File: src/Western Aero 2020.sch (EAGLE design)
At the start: 85 parts, among them U1 7806, U2 7805, U3 TEENSY_3.5_DIL+4, U5 SPARKFUN_MPU9250_IMU, U6 ADAFRUIT_MPL3115A2_BAROMETER, U7 ADAFRUIT_INA219_BATTERY_SENSOR, U8 ADAFRUIT_RFM95W_LORA_RADIO, U9 ADAFRUIT_MTK3339_GPS

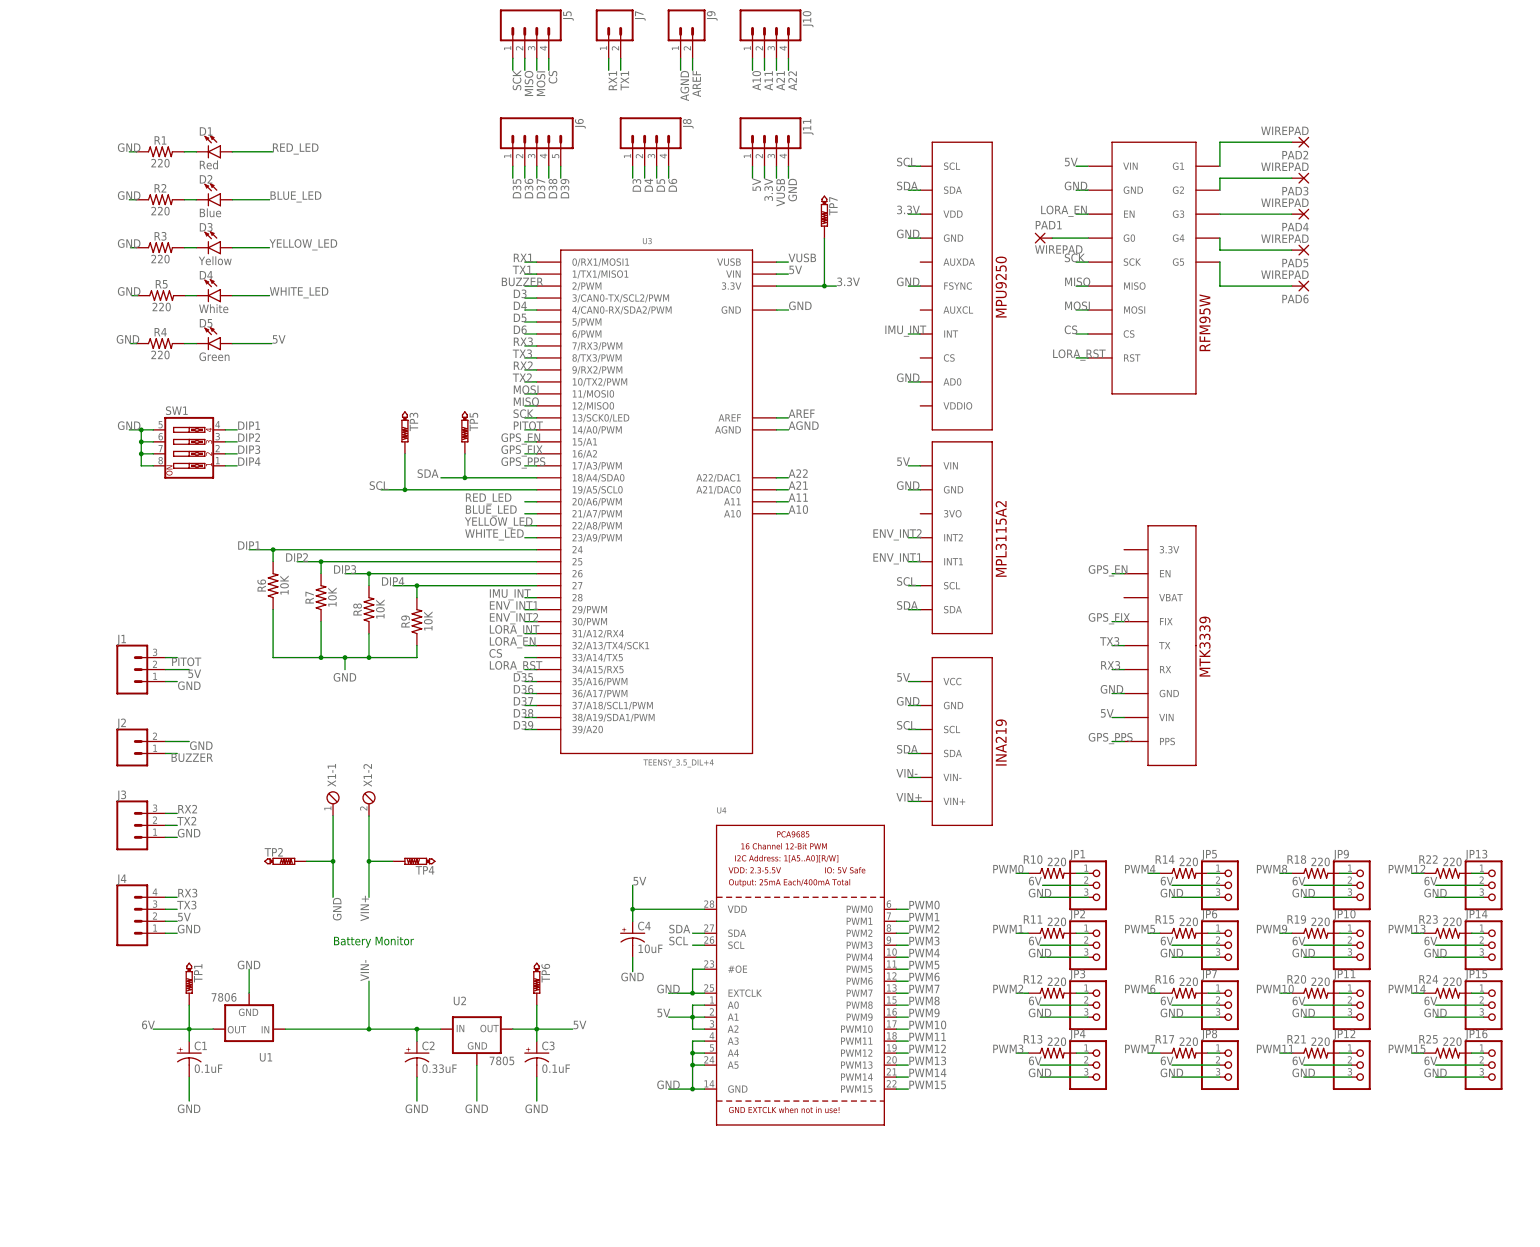
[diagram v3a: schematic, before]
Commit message: Add new voltage regulator
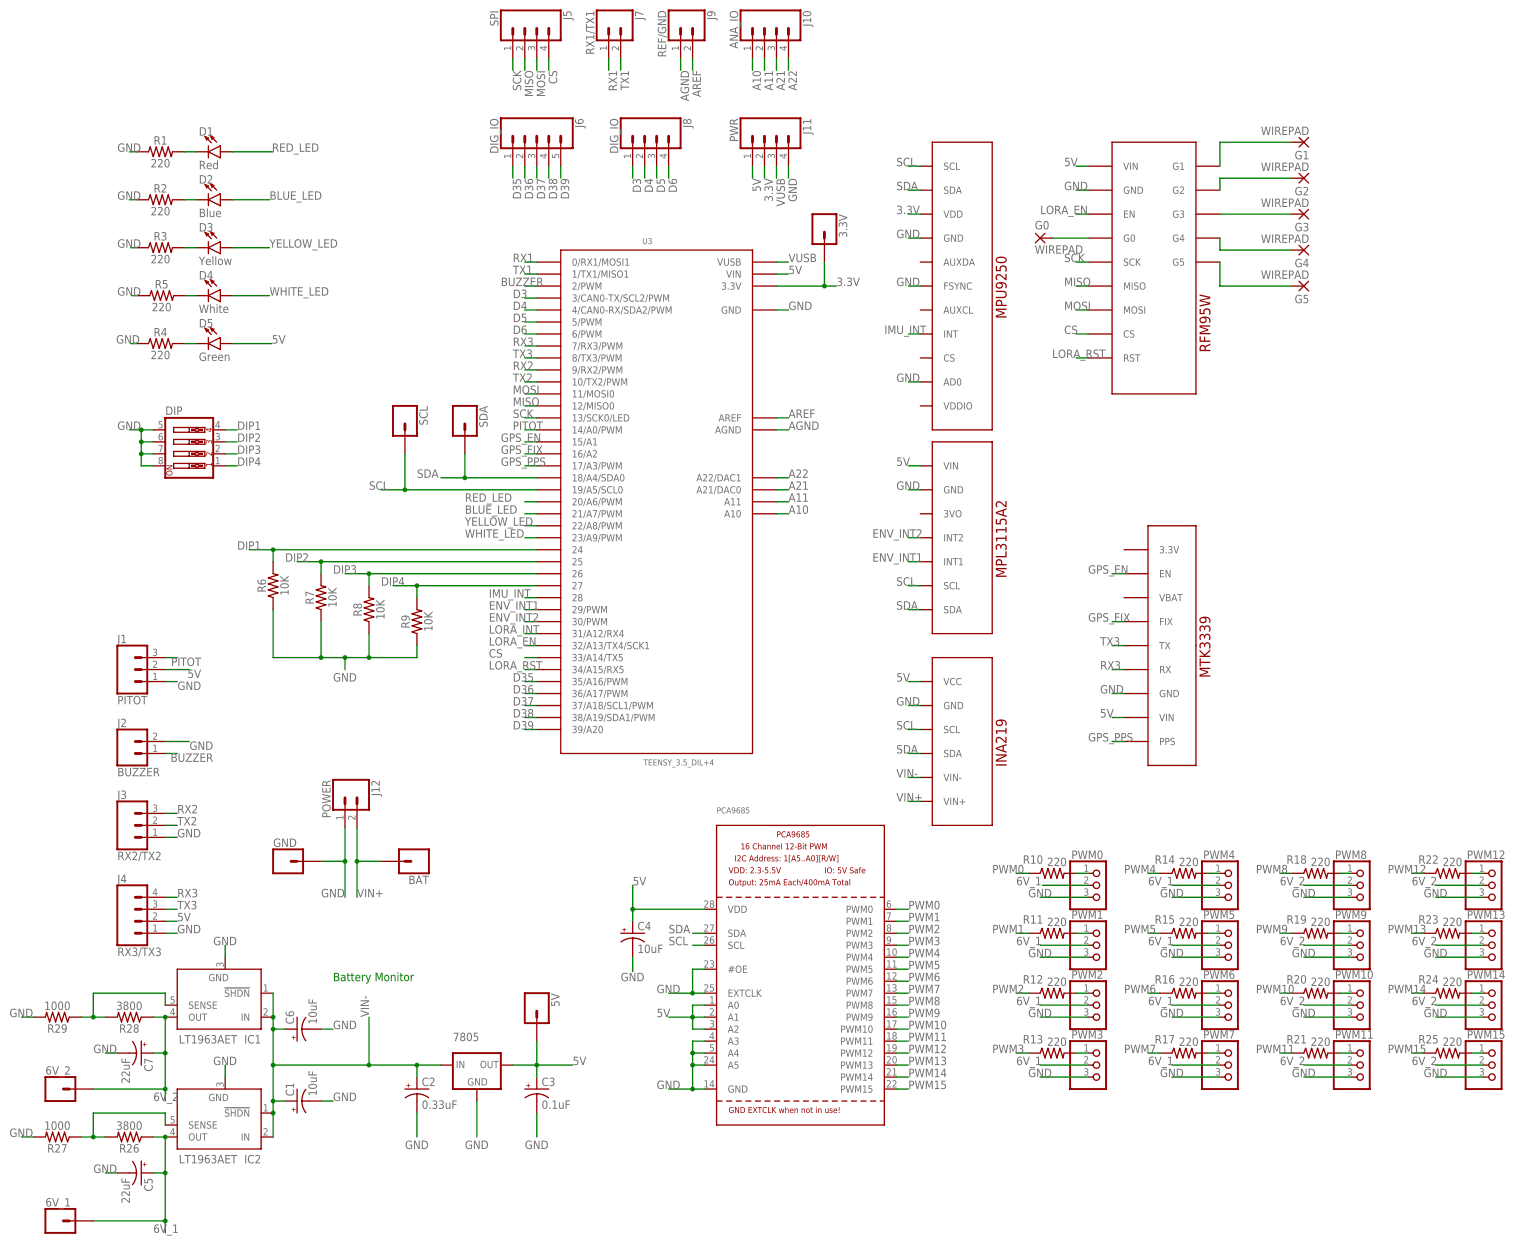
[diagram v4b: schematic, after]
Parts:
- removed TP1, TP2, TP3, TP4, TP5, TP6, TP7: PTR1PAD1-13, testpad:PTR1PAD1-13
- removed U1: 7806, SparkFun-IC-Power:V_REG_78XXSINK
- removed U2: 7805, SparkFun-IC-Power:V_REG_78XXSINK
- removed X1: (no value), con-phoenix-254:MPT2
- added 3.3V, 5V, 6V_1, 6V_2, BAT, GND, SCL, SDA: (no value), SparkFun-Connectors:CONN_01
- added 7805: 7805, SparkFun-IC-Power:V_REG_78XXSINK
- added C5, C7: 22uF, SparkFun-Capacitors:10UF-POLAR-RADIAL-2.5MM-25V-20%
- added C6: 10uF, SparkFun-Capacitors:10UF-POLAR-RADIAL-2.5MM-25V-20%
- added IC1, IC2: LT1963AET, linear-technology:LT1963AET
- added J12: POWER, SparkFun-Connectors:CONN_02
- added R26, R28: 3800, SparkFun-Resistors:330OHM-HORIZ-1/10W-5%
- added R27, R29: 1000, SparkFun-Resistors:330OHM-HORIZ-1/10W-5%
- C1: value 0.1uF -> 10uF
- J1: value (none) -> PITOT
- J10: value (none) -> ANA_IO
- J11: value (none) -> PWR
- J2: value (none) -> BUZZER
- J3: value (none) -> RX2/TX2
- J4: value (none) -> RX3/TX3
- J5: value (none) -> SPI
- J6, J8: value (none) -> DIG_IO
- J7: value (none) -> RX1/TX1
- J9: value (none) -> REF/GND
- JP1: value (none) -> PWM0
- JP10: value (none) -> PWM9
- JP11: value (none) -> PWM10
- JP12: value (none) -> PWM11
- JP13: value (none) -> PWM12
- JP14: value (none) -> PWM13
- JP15: value (none) -> PWM14
- JP16: value (none) -> PWM15
- JP2: value (none) -> PWM1
- JP3: value (none) -> PWM2
- JP4: value (none) -> PWM3
- JP5: value (none) -> PWM4
- JP6: value (none) -> PWM5
- JP7: value (none) -> PWM6
- JP8: value (none) -> PWM7
- JP9: value (none) -> PWM8
- renumbered PAD1 to G0, PAD2 to G1, PAD3 to G2, PAD4 to G3, PAD5 to G4, PAD6 to G5, SW1 to DIP, U4 to PCA9685
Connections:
- removed net 6V: C1.+, JP1.2, JP10.2, JP11.2, JP12.2, JP13.2, JP14.2, JP15.2, JP16.2, JP2.2, JP3.2, JP4.2, JP5.2, JP6.2, JP7.2, JP8.2, JP9.2, TP1.TP, U1.OUT
- new net 6V_1: 6V_1.1, C5.+, IC2.OUT, JP1.2, JP2.2, JP3.2, JP4.2, JP5.2, JP6.2, JP7.2, JP8.2, R26.1
- new net 6V_2: 6V_2.1, C7.+, IC1.OUT, JP10.2, JP11.2, JP12.2, JP13.2, JP14.2, JP15.2, JP16.2, JP9.2, R28.1
- new net N$28: IC1.SENSE, R28.2, R29.1
- new net N$29: IC2.SENSE, R26.2, R27.1
- net 3.3V: now also 3.3V.1; no longer TP7.TP
- net 5V: now also 5V.1, 7805.OUT; no longer TP6.TP, U2.OUT
- net GND: now also 7805.GND, C5.-, C6.-, C7.-, GND.1, IC1.GND, IC2.GND, J12.1, R27.2, R29.2; no longer TP2.TP, U1.GND, U2.GND, X1-1.1
- net SCL: now also SCL.1; no longer TP3.TP
- net SDA: now also SDA.1; no longer TP5.TP
- net VIN+: now also BAT.1, J12.2; no longer TP4.TP, X1-2.1
- net VIN-: now also 7805.IN, C1.+, C6.+, IC1.!SHDN, IC1.IN, IC2.!SHDN, IC2.IN; no longer U1.IN, U2.IN
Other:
- moved on the sheet: C1, C2, C3

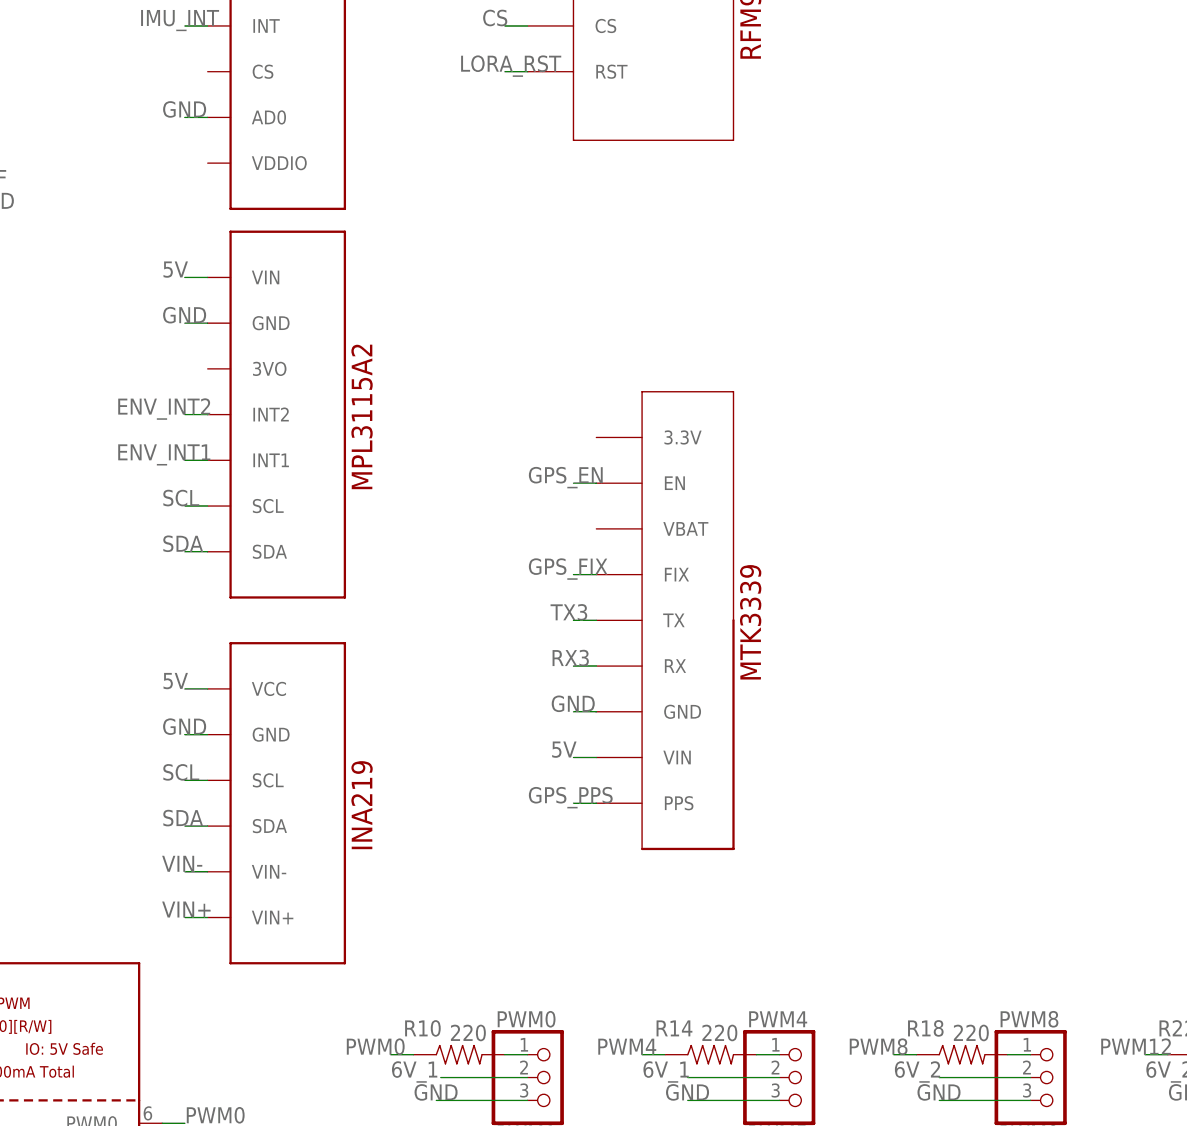
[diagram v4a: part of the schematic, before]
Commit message: Changed test point parts. Updated parts list. Adjusted board layout.
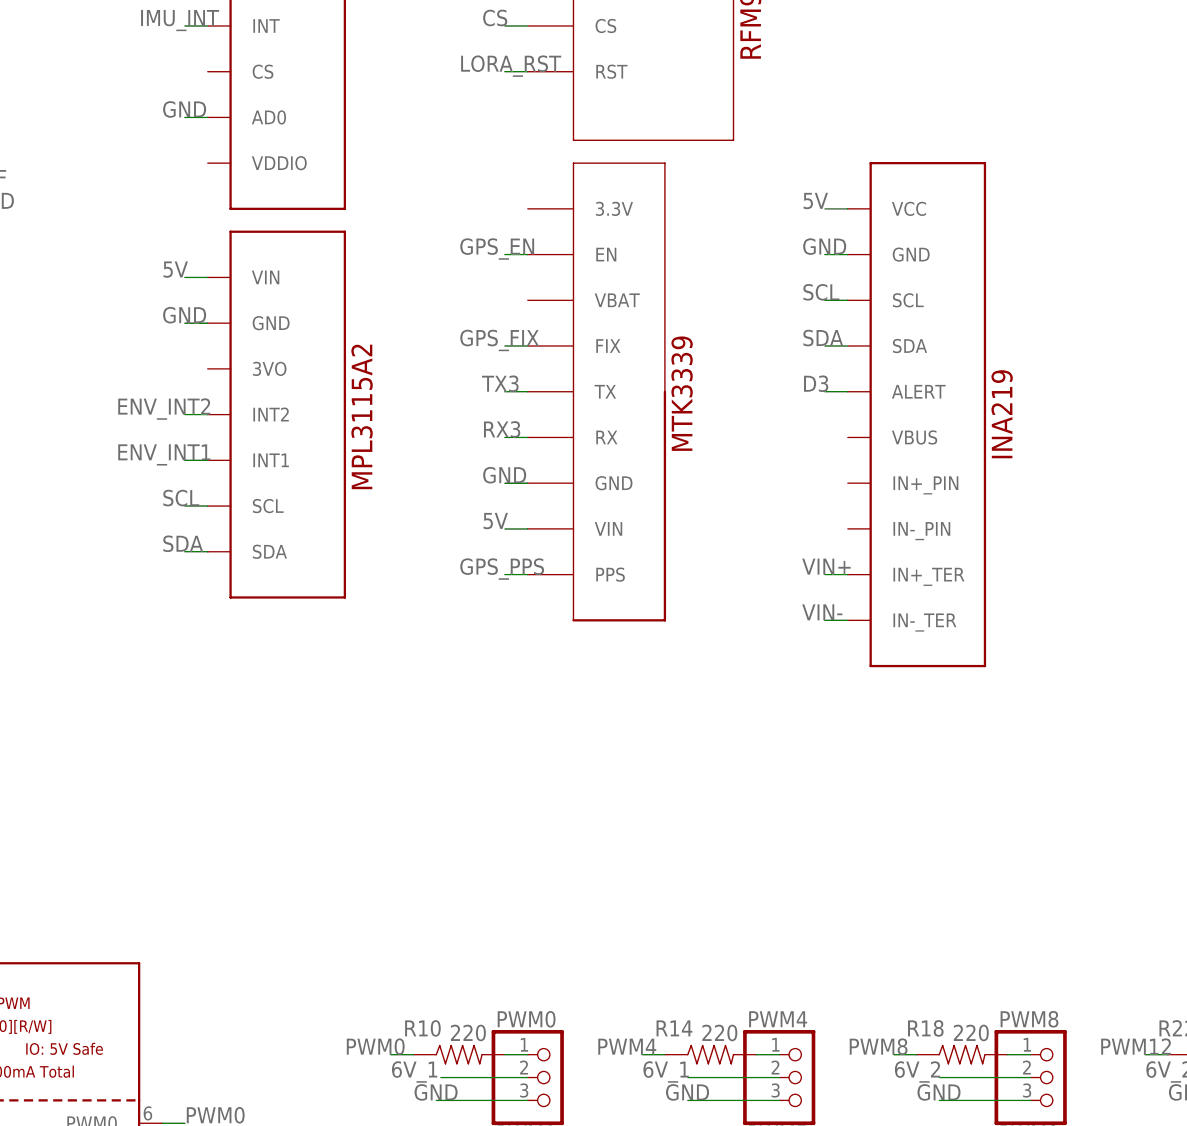
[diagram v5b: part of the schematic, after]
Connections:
- net D3: now also U7.ALERT
- net VIN+: now also U7.IN+_TER; no longer U7.VIN+
- net VIN-: now also U7.IN-_TER; no longer U7.VIN-
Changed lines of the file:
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@@
 <instance part="U8" gate="G$1" x="121.92" y="195.58" smashed="yes" rot="R270"/>
 <instance part="U6" gate="G$1" x="83.82" y="132.08" smashed="yes" rot="R270"/>
-<instance part="U7" gate="G$1" x="83.82" y="86.36" smashed="yes" rot="R270"/>
+<instance part="U7" gate="G$1" x="154.94" y="139.7" smashed="yes" rot="R270"/>
 <instance part="J2" gate="G$1" x="-86.36" y="66.04" smashed="yes">
 <attribute name="VALUE" x="-88.9" y="61.214" size="1.778" layer="96" font="vector"/>
@@
 <attribute name="NAME" x="-88.9" y="38.608" size="1.778" layer="95" font="vector"/>
 </instance>
-<instance part="U9" gate="G$1" x="137.16" y="114.3" smashed="yes" rot="R270"/>
+<instance part="U9" gate="G$1" x="129.54" y="139.7" smashed="yes" rot="R270"/>
 <instance part="J7" gate="G$1" x="15.24" y="220.98" smashed="yes" rot="R270">
 <attribute name="VALUE" x="10.414" y="223.52" size="1.778" layer="96" font="vector" rot="R270"/>
@@
 <nets>
 <net name="VIN+" class="0">
-<segment>
-<pinref part="U7" gate="G$1" pin="VIN+"/>
-<wire x1="81.28" y1="55.88" x2="78.74" y2="55.88" width="0.1524" layer="91"/>
-<label x="76.2" y="55.88" size="1.778" layer="95"/>
-</segment>
 <segment>
 <label x="-38.1" y="35.56" size="1.778" layer="95"/>
@@
 <junction x="-38.1" y="43.18"/>
 </segment>
+<segment>
+<pinref part="U7" gate="G$1" pin="IN+_TER"/>
+<wire x1="152.4" y1="93.98" x2="149.86" y2="93.98" width="0.1524" layer="91"/>
+<label x="147.32" y="93.98" size="1.778" layer="95"/>
+</segment>
 </net>
 <net name="3.3V" class="0">
@@
 <segment>
 <pinref part="U7" gate="G$1" pin="GND"/>
-<wire x1="81.28" y1="76.2" x2="78.74" y2="76.2" width="0.1524" layer="91"/>
-<label x="76.2" y="76.2" size="1.778" layer="95"/>
+<wire x1="152.4" y1="129.54" x2="149.86" y2="129.54" width="0.1524" layer="91"/>
+<label x="147.32" y="129.54" size="1.778" layer="95"/>
 </segment>
 <segment>
@@
 <segment>
 <pinref part="U9" gate="G$1" pin="GND"/>
-<wire x1="124.46" y1="78.74" x2="121.92" y2="78.74" width="0.1524" layer="91"/>
-<label x="119.38" y="78.74" size="1.778" layer="95"/>
+<wire x1="116.84" y1="104.14" x2="114.3" y2="104.14" width="0.1524" layer="91"/>
+<label x="111.76" y="104.14" size="1.778" layer="95"/>
 </segment>
 <segment>
@@
 <segment>
 <pinref part="U7" gate="G$1" pin="SDA"/>
-<wire x1="81.28" y1="66.04" x2="78.74" y2="66.04" width="0.1524" layer="91"/>
-<label x="76.2" y="66.04" size="1.778" layer="95"/>
+<wire x1="152.4" y1="119.38" x2="149.86" y2="119.38" width="0.1524" layer="91"/>
+<label x="147.32" y="119.38" size="1.778" layer="95"/>
 </segment>
 <segment>
@@
 <segment>
 <pinref part="U7" gate="G$1" pin="SCL"/>
-<wire x1="81.28" y1="71.12" x2="78.74" y2="71.12" width="0.1524" layer="91"/>
-<label x="76.2" y="71.12" size="1.778" layer="95"/>
+<wire x1="152.4" y1="124.46" x2="149.86" y2="124.46" width="0.1524" layer="91"/>
+<label x="147.32" y="124.46" size="1.778" layer="95"/>
 </segment>
 <segment>
@@
 <segment>
 <pinref part="U7" gate="G$1" pin="VCC"/>
-<wire x1="81.28" y1="81.28" x2="78.74" y2="81.28" width="0.1524" layer="91"/>
-<label x="76.2" y="81.28" size="1.778" layer="95"/>
+<wire x1="152.4" y1="134.62" x2="149.86" y2="134.62" width="0.1524" layer="91"/>
+<label x="147.32" y="134.62" size="1.778" layer="95"/>
 </segment>
 <segment>
@@
 <segment>
 <pinref part="U9" gate="G$1" pin="VIN"/>
-<wire x1="124.46" y1="73.66" x2="121.92" y2="73.66" width="0.1524" layer="91"/>
-<label x="119.38" y="73.66" size="1.778" layer="95"/>
+<wire x1="116.84" y1="99.06" x2="114.3" y2="99.06" width="0.1524" layer="91"/>
+<label x="111.76" y="99.06" size="1.778" layer="95"/>
 </segment>
 <segment>
@@
 </net>
 <net name="VIN-" class="0">
-<segment>
-<pinref part="U7" gate="G$1" pin="VIN-"/>
-<wire x1="81.28" y1="60.96" x2="78.74" y2="60.96" width="0.1524" layer="91"/>
-<label x="76.2" y="60.96" size="1.778" layer="95"/>
-</segment>
 <segment>
 <wire x1="-25.4" y1="0" x2="-25.4" y2="-2.54" width="0.1524" layer="91"/>
@@
 <junction x="-55.88" y="7.62"/>
 </segment>
+<segment>
+<pinref part="U7" gate="G$1" pin="IN-_TER"/>
+<wire x1="152.4" y1="88.9" x2="149.86" y2="88.9" width="0.1524" layer="91"/>
+<label x="147.32" y="88.9" size="1.778" layer="95"/>
+</segment>
 </net>
 <net name="WHITE_LED" class="0">
@@
 <segment>
 <pinref part="U9" gate="G$1" pin="RX"/>
-<wire x1="124.46" y1="83.82" x2="121.92" y2="83.82" width="0.1524" layer="91"/>
-<label x="119.38" y="83.82" size="1.778" layer="95"/>
+<wire x1="116.84" y1="109.22" x2="114.3" y2="109.22" width="0.1524" layer="91"/>
+<label x="111.76" y="109.22" size="1.778" layer="95"/>
 </segment>
 </net>
@@
 <segment>
 <pinref part="U9" gate="G$1" pin="TX"/>
-<wire x1="124.46" y1="88.9" x2="121.92" y2="88.9" width="0.1524" layer="91"/>
-<label x="119.38" y="88.9" size="1.778" layer="95"/>
+<wire x1="116.84" y1="114.3" x2="114.3" y2="114.3" width="0.1524" layer="91"/>
+<label x="111.76" y="114.3" size="1.778" layer="95"/>
 </segment>
 </net>
@@
 <segment>
 <pinref part="U9" gate="G$1" pin="EN"/>
-<wire x1="124.46" y1="104.14" x2="121.92" y2="104.14" width="0.1524" layer="91"/>
-<label x="116.84" y="104.14" size="1.778" layer="95"/>
+<wire x1="116.84" y1="129.54" x2="114.3" y2="129.54" width="0.1524" layer="91"/>
+<label x="109.22" y="129.54" size="1.778" layer="95"/>
 </segment>
 <segment>
@@
 <segment>
 <pinref part="U9" gate="G$1" pin="FIX"/>
-<wire x1="124.46" y1="93.98" x2="121.92" y2="93.98" width="0.1524" layer="91"/>
-<label x="116.84" y="93.98" size="1.778" layer="95"/>
+<wire x1="116.84" y1="119.38" x2="114.3" y2="119.38" width="0.1524" layer="91"/>
+<label x="109.22" y="119.38" size="1.778" layer="95"/>
 </segment>
 <segment>
@@
 <segment>
 <pinref part="U9" gate="G$1" pin="PPS"/>
-<wire x1="124.46" y1="68.58" x2="121.92" y2="68.58" width="0.1524" layer="91"/>
-<label x="116.84" y="68.58" size="1.778" layer="95"/>
+<wire x1="116.84" y1="93.98" x2="114.3" y2="93.98" width="0.1524" layer="91"/>
+<label x="109.22" y="93.98" size="1.778" layer="95"/>
 </segment>
 <segment>
@@
 <label x="-5.08" y="162.56" size="1.778" layer="95"/>
 </segment>
-</net>
+<segment>
+<pinref part="U7" gate="G$1" pin="ALERT"/>
+<wire x1="152.4" y1="114.3" x2="149.86" y2="114.3" width="0.1524" layer="91"/>
+<label x="147.32" y="114.3" size="1.778" layer="95"/>
+</segment>
+</net>
